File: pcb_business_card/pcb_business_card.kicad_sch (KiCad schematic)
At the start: 1 part, among them U1 ATtiny85-20M

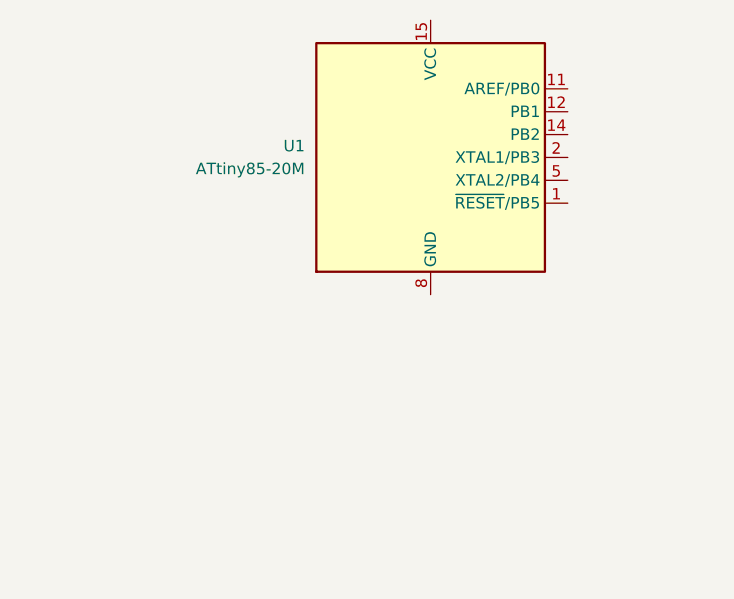
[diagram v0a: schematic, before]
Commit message: adding some more schematic symbols
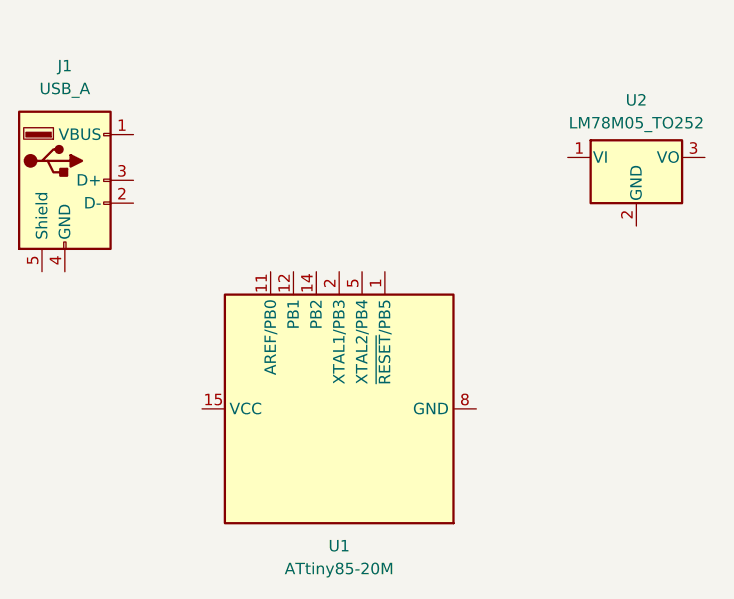
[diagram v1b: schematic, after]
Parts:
- added J1: USB_A, symbol Connector:USB_A
- added U2: LM78M05_TO252, Package_TO_SOT_SMD:TO-252-2, symbol Regulator_Linear:LM78M05_TO252
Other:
- moved on the sheet: U1
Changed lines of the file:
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@@
 (kicad_sch (version 20230121) (generator eeschema)
   (paper "A4")
-  (symbol (lib_id "MCU_Microchip_ATtiny:ATtiny85-20M") (at 96.52 58.42 0) (unit 1)
+  (symbol (lib_id "Regulator_Linear:LM78M05_TO252") (at 119.38 58.42 0) (unit 1)
     (in_bom yes) (on_board yes) (dnp no) (fields_autoplaced)
-    (property "Reference" "U1" (at 82.55 57.15 0)
-      (effects (font (size 1.27 1.27)) (justify right))
+    (property "Reference" "U2" (at 119.38 52.07 0)
+      (effects (font (size 1.27 1.27)))
     )
-    (property "Value" "ATtiny85-20M" (at 82.55 59.69 0)
-      (effects (font (size 1.27 1.27)) (justify right))
+    (property "Value" "LM78M05_TO252" (at 119.38 54.61 0)
+      (effects (font (size 1.27 1.27)))
     )
-    (property "Footprint" "Package_DFN_QFN:QFN-20-1EP_4x4mm_P0.5mm_EP2.6x2.6mm" (at 96.52 58.42 0)
+    (property "Footprint" "Package_TO_SOT_SMD:TO-252-2" (at 119.38 52.705 0)
       (effects (font (size 1.27 1.27) italic) hide)
     )
-    (property "Datasheet" "http://ww1.microchip.com/downloads/en/DeviceDoc/atmel-2586-avr-8-bit-microcontroller-attiny25-attiny45-attiny85_datasheet.pdf" (at 96.52 58.42 0)
+    (property "Datasheet" "https://www.onsemi.com/pub/Collateral/MC78M00-D.PDF" (at 119.38 59.69 0)
       (effects (font (size 1.27 1.27)) hide)
     )
+    (pin "1")
+    (pin "2")
+    (pin "3")
+    (instances
+      (project "pcb_business_card"
+        (path "/53a7bf37-3aa1-4415-a399-d72f9eaf997c"
+          (reference "U2") (unit 1)
+        )
+      )
+    )
+  )
+  (symbol (lib_id "Connector:USB_A") (at 55.88 60.96 0) (unit 1)
+    (in_bom yes) (on_board yes) (dnp no) (fields_autoplaced)
+    (property "Reference" "J1" (at 55.88 48.26 0)
+      (effects (font (size 1.27 1.27)))
+    )
+    (property "Value" "USB_A" (at 55.88 50.8 0)
+      (effects (font (size 1.27 1.27)))
+    )
+    (property "Footprint" "" (at 59.69 62.23 0)
+      (effects (font (size 1.27 1.27)) hide)
+    )
+    (property "Datasheet" " ~" (at 59.69 62.23 0)
+      (effects (font (size 1.27 1.27)) hide)
+    )
+    (pin "1")
+    (pin "2")
+    (pin "3")
+    (pin "4")
+    (pin "5")
+    (instances
+      (project "pcb_business_card"
+        (path "/53a7bf37-3aa1-4415-a399-d72f9eaf997c"
+          (reference "J1") (unit 1)
+        )
+      )
+    )
+  )
+  (symbol (lib_id "MCU_Microchip_ATtiny:ATtiny85-20M") (at 86.36 86.36 90) (unit 1)
+    (in_bom yes) (on_board yes) (dnp no) (fields_autoplaced)
+    (property "Reference" "U1" (at 86.36 101.6 90)
+      (effects (font (size 1.27 1.27)))
+    )
+    (property "Value" "ATtiny85-20M" (at 86.36 104.14 90)
+      (effects (font (size 1.27 1.27)))
+    )
+    (property "Footprint" "Package_DFN_QFN:QFN-20-1EP_4x4mm_P0.5mm_EP2.6x2.6mm" (at 86.36 86.36 0)
+      (effects (font (size 1.27 1.27) italic) hide)
+    )
+    (property "Datasheet" "http://ww1.microchip.com/downloads/en/DeviceDoc/atmel-2586-avr-8-bit-microcontroller-attiny25-attiny45-attiny85_datasheet.pdf" (at 86.36 86.36 0)
+      (effects (font (size 1.27 1.27)) hide)
+    )
